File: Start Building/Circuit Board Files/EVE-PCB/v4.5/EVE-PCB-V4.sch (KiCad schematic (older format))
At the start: 37 parts, among them J1 PJ-102AH, J2 2x20 Male Header, J3 1725669, Q1 UA7805CKCT, Q6 DMN10H220L-7, Q7 DMN10H220L-7, U1 PCA9685PW, U2 ADS1115IDGSR, U3 LM324DR

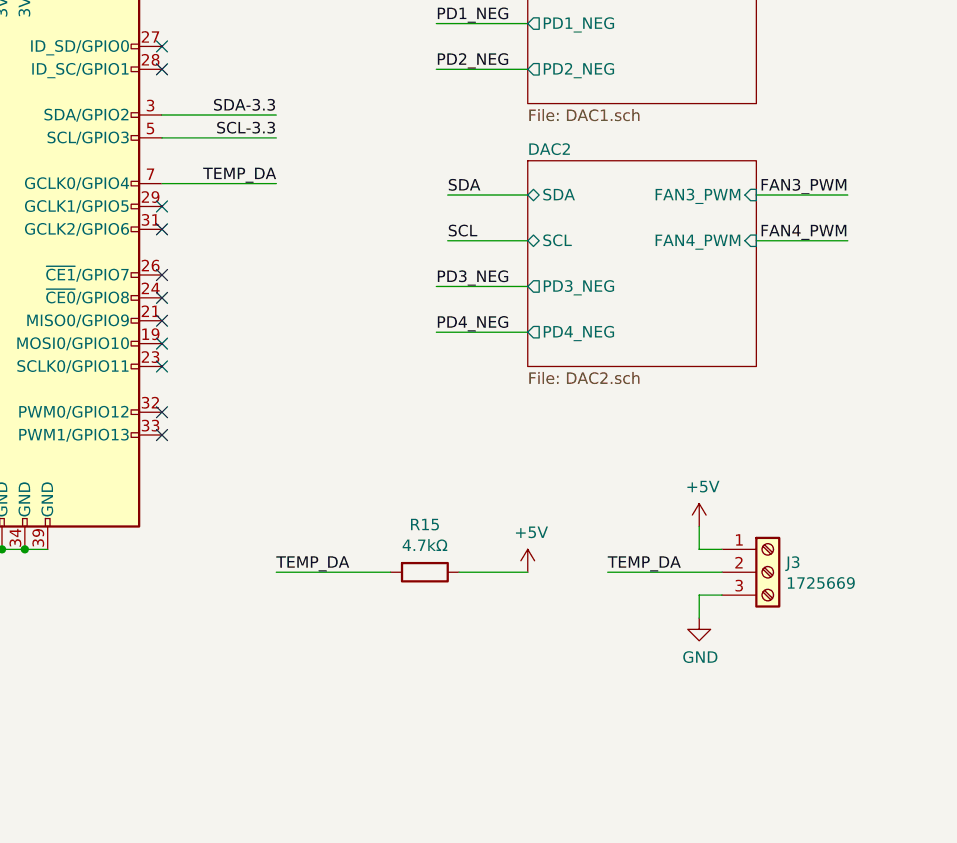
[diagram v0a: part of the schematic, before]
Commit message: PCB v4.5 temp sensor PCB addition
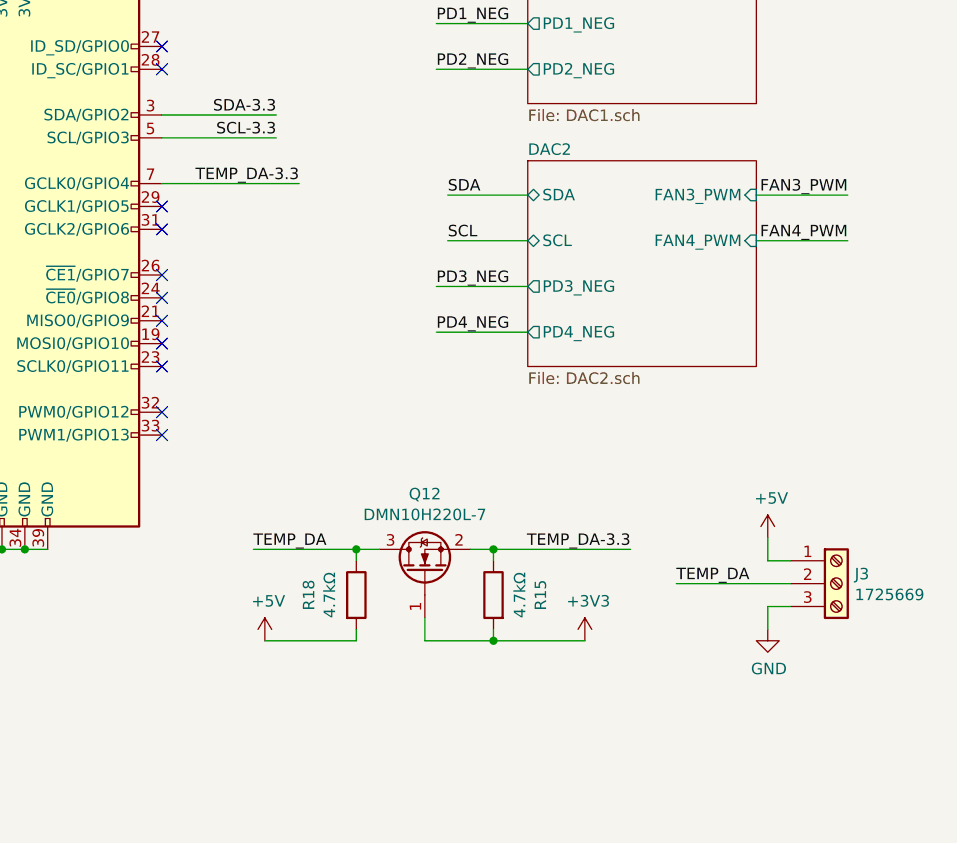
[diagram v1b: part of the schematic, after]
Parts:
- added Q12: DMN10H220L-7, Package_TO_SOT_SMD:SOT-23, symbol Transistor_FET:DMN10H220L
- added R18: 4.7kΩ, Resistor_SMD:R_0402_1005Metric, symbol Device:R
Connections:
- net +3V3: now also R15.2, Q12.1 (G)
- net +5V: now also R18.2; no longer R15.1
- net TEMP_DA: now also Q12.3 (D), R18.1; no longer J2.7 (GCLK0/GPIO4), R15.2
- new net TEMP_DA-3.3: J2.7 (GCLK0/GPIO4), Q12.2 (S), R15.1
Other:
- moved on the sheet: J3, R15
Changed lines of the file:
@@
 L Connector:Screw_Terminal_01x03 J3
 U 1 1 5EC87689
-P 10200 5600
-F 0 "J3" H 10280 5642 50  0000 L CNN
-F 1 "1725669" H 10280 5551 50  0000 L CNN
-F 2 "1725669andothers:1725669" H 10200 5600 50  0001 C CNN
-F 3 "1935174" H 10200 5600 50  0001 C CNN
-	1    10200 5600
+P 10500 5650
+F 0 "J3" H 10580 5692 50  0000 L CNN
+F 1 "1725669" H 10580 5601 50  0000 L CNN
+F 2 "1725669andothers:1725669" H 10500 5650 50  0001 C CNN
+F 3 "1935174" H 10500 5650 50  0001 C CNN
+	1    10500 5650
 	1    0    0    -1
 $EndComp
@@
 L EVE-PCB-V4-rescue:+5V-power-EVE-PCB-rescue #PWR07
 U 1 1 5ECA1474
-P 9900 5400
-F 0 "#PWR07" H 9900 5250 50  0001 C CNN
-F 1 "+5V" H 9915 5573 50  0000 C CNN
-F 2 "" H 9900 5400 50  0001 C CNN
-F 3 "" H 9900 5400 50  0001 C CNN
-	1    9900 5400
+P 10200 5450
+F 0 "#PWR07" H 10200 5300 50  0001 C CNN
+F 1 "+5V" H 10215 5623 50  0000 C CNN
+F 2 "" H 10200 5450 50  0001 C CNN
+F 3 "" H 10200 5450 50  0001 C CNN
+	1    10200 5450
 	1    0    0    -1
 $EndComp
-Text Label 8050 3900 2    50   ~ 0
+Text Label 8150 3900 2    50   ~ 0
+TEMP_DA-3.3
+Text Label 9800 5650 0    50   ~ 0
 TEMP_DA
 Wire Wire Line
-	8050 3900 7550 3900
-Text Label 9500 5600 0    50   ~ 0
-TEMP_DA
+	10300 5650 9800 5650
 Wire Wire Line
-	10000 5600 9500 5600
+	10200 5450 10200 5550
 Wire Wire Line
-	9900 5400 9900 5500
-Wire Wire Line
-	9900 5500 10000 5500
+	10200 5550 10300 5550
 $Comp
 L EVE-PCB-V4-rescue:GND-power-EVE-PCB-rescue #PWR08
 U 1 1 5ED40817
-P 9900 5800
-F 0 "#PWR08" H 9900 5550 50  0001 C CNN
-F 1 "GND" H 9905 5627 50  0000 C CNN
-F 2 "" H 9900 5800 50  0001 C CNN
-F 3 "" H 9900 5800 50  0001 C CNN
-	1    9900 5800
+P 10200 5850
+F 0 "#PWR08" H 10200 5600 50  0001 C CNN
+F 1 "GND" H 10205 5677 50  0000 C CNN
+F 2 "" H 10200 5850 50  0001 C CNN
+F 3 "" H 10200 5850 50  0001 C CNN
+	1    10200 5850
 	1    0    0    -1
 $EndComp
 Wire Wire Line
-	9900 5800 9900 5700
+	10200 5850 10200 5750
 Wire Wire Line
-	9900 5700 10000 5700
-Text Label 8050 5600 0    50   ~ 0
-TEMP_DA
-Wire Wire Line
-	8550 5600 8050 5600
+	10200 5750 10300 5750
 $Comp
 L Device:R R15
 U 1 1 5ED69B49
-P 8700 5600
-F 0 "R15" V 8493 5600 50  0000 C CNN
-F 1 "4.7kΩ" V 8584 5600 50  0000 C CNN
-F 2 "Resistor_SMD:R_0402_1005Metric" V 8630 5600 50  0001 C CNN
-F 3 "0402WGF4701TCE" H 8700 5600 50  0001 C CNN
-F 4 "C25900" V 8700 5600 50  0001 C CNN "LCSC"
-F 5 "0402" H 8700 5600 50  0001 C CNN "Package"
-F 6 "Low" V 8700 5600 50  0001 C CNN "Power"
-	1    8700 5600
-	0    1    1    0
+P 9000 5700
+F 0 "R15" V 8793 5700 50  0000 C CNN
+F 1 "4.7kΩ" V 8884 5700 50  0000 C CNN
+F 2 "Resistor_SMD:R_0402_1005Metric" V 8930 5700 50  0001 C CNN
+F 3 "0402WGF4701TCE" H 9000 5700 50  0001 C CNN
+F 4 "C25900" V 9000 5700 50  0001 C CNN "LCSC"
+F 5 "0402" H 9000 5700 50  0001 C CNN "Package"
+F 6 "Low" V 9000 5700 50  0001 C CNN "Power"
+	1    9000 5700
+	-1   0    0    -1
 $EndComp
+Wire Wire Line
+	8900 5500 9000 5500
 $Comp
-L EVE-PCB-V4-rescue:+5V-power-EVE-PCB-rescue #PWR03
-U 1 1 5ED75219
-P 9150 5600
-F 0 "#PWR03" H 9150 5450 50  0001 C CNN
-F 1 "+5V" H 9165 5773 50  0000 C CNN
-F 2 "" H 9150 5600 50  0001 C CNN
-F 3 "" H 9150 5600 50  0001 C CNN
-	1    9150 5600
+L EVE-PCB-V4-rescue:+3V3-power-EVE-PCB-rescue #PWR016
+U 1 1 5EDD4AD6
+P 9400 5900
+F 0 "#PWR016" H 9400 5750 50  0001 C CNN
+F 1 "+3V3" H 9415 6073 50  0000 C CNN
+F 2 "" H 9400 5900 50  0001 C CNN
+F 3 "" H 9400 5900 50  0001 C CNN
+	1    9400 5900
 	1    0    0    -1
 $EndComp
 Wire Wire Line
-	8850 5600 9150 5600
+	9000 5550 9000 5500
+Wire Wire Line
+	9000 5850 9000 5900
+Connection ~ 9000 5900
+$Comp
+L EVE-PCB-V4-rescue:+5V-power-EVE-PCB-rescue #PWR03
+U 1 1 5EDD4AE0
+P 8000 5900
+F 0 "#PWR03" H 8000 5750 50  0001 C CNN
+F 1 "+5V" H 8015 6073 50  0000 C CNN
+F 2 "" H 8000 5900 50  0001 C CNN
+F 3 "" H 8000 5900 50  0001 C CNN
+	1    8000 5900
+	1    0    0    -1
+$EndComp
+Wire Wire Line
+	8400 5900 8400 5850
+Wire Wire Line
+	8400 5550 8400 5500
+Connection ~ 8400 5500
+Wire Wire Line
+	8400 5500 8500 5500
+Wire Wire Line
+	8000 5900 8400 5900
+Wire Wire Line
+	9000 5900 9400 5900
+Connection ~ 9000 5500
+$Comp
+L Transistor_FET:DMN10H220L Q12
+U 1 1 5EDD4B03
+P 8700 5600
+F 0 "Q12" V 9042 5600 50  0000 C CNN
+F 1 "DMN10H220L-7" V 8951 5600 50  0000 C CNN
+F 2 "Package_TO_SOT_SMD:SOT-23" H 8900 5525 50  0001 L CIN
+F 3 "DMN10H220L-7" H 8700 5600 50  0001 L CNN
+F 4 "C102615" H 8700 5600 50  0001 C CNN "LCSC"
+F 5 "SOT-23-3" H 8700 5600 50  0001 C CNN "Package"
+	1    8700 5600
+	0    -1   -1   0
+$EndComp
+Wire Wire Line
+	8700 5800 8700 5900
+Wire Wire Line
+	8700 5900 9000 5900
+$Comp
+L Device:R R18
+U 1 1 5EE07A53
+P 8400 5700
+F 0 "R18" V 8193 5700 50  0000 C CNN
+F 1 "4.7kΩ" V 8284 5700 50  0000 C CNN
+F 2 "Resistor_SMD:R_0402_1005Metric" V 8330 5700 50  0001 C CNN
+F 3 "0402WGF4701TCE" H 8400 5700 50  0001 C CNN
+F 4 "C25900" V 8400 5700 50  0001 C CNN "LCSC"
+F 5 "0402" H 8400 5700 50  0001 C CNN "Package"
+F 6 "Low" V 8400 5700 50  0001 C CNN "Power"
+	1    8400 5700
+	1    0    0    -1
+$EndComp
+Text Label 7950 5500 0    50   ~ 0
+TEMP_DA
+Wire Wire Line
+	7950 5500 8400 5500
+Text Label 9600 5500 2    50   ~ 0
+TEMP_DA-3.3
+Wire Wire Line
+	9000 5500 9600 5500
+Wire Wire Line
+	7550 3900 8150 3900
 $EndSCHEMATC

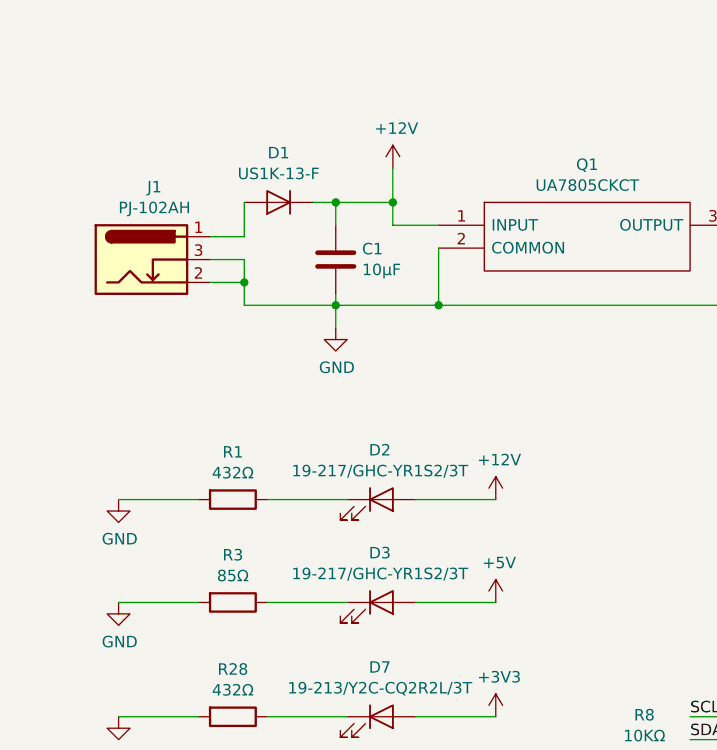
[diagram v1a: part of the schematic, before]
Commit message: Updates to v4.5 and include support for ADS1115
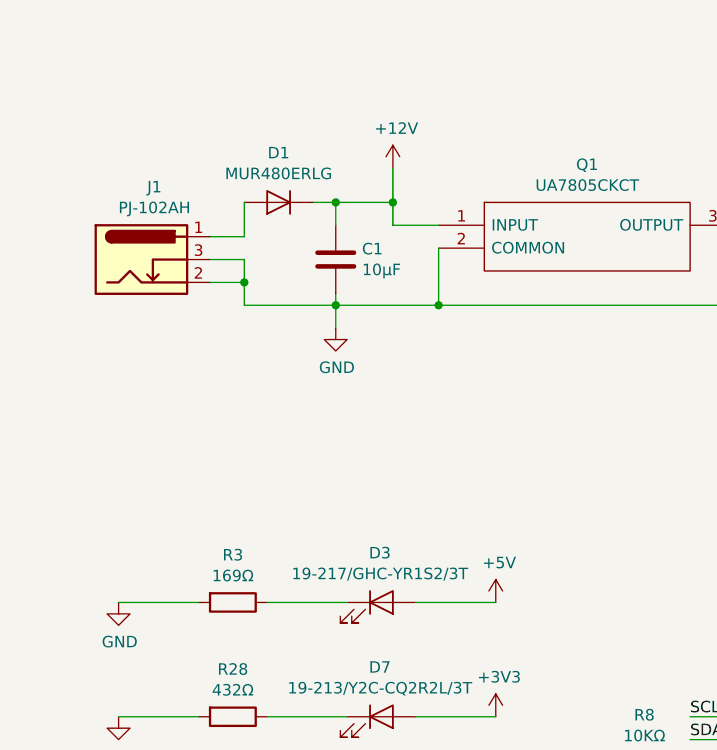
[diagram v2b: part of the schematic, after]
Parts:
- removed D2: 19-217/GHC-YR1S2/3T, LED_SMD:LED_0603_1608Metric, symbol Device:LED
- removed R1: 432Ω, Resistor_SMD:R_1206_3216Metric, symbol Device:R
- C6: footprint Capacitor_SMD:C_0402_1005Metric -> Capacitor_SMD:C_0603_1608Metric; LCSC C29266 -> C5673; Package 0402 -> 0603
- D1: value US1K-13-F -> MUR480ERLG; footprint Diode_SMD:D_SMA -> Diode_THT:D_DO-201AE_P3.81mm_Vertical_AnodeUp; LCSC C110532 -> (none)
- R3: value 85Ω -> 169Ω; LCSC C17843 -> C17489; Power 0.034 -> 0.017
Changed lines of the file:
@@
 	2350 3450 2550 3450
-$Comp
-L EVE-PCB-V4-rescue:+12V-power-EVE-PCB-rescue #PWR?
-U 1 1 5EBD3BD1
-P 2800 4650
-AR Path="/5CA7DFAE/5EBD3BD1" Ref="#PWR?"  Part="1"
-AR Path="/5EBD3BD1" Ref="#PWR06"  Part="1"
-F 0 "#PWR06" H 2800 4500 50  0001 C CNN
-F 1 "+12V" H 2815 4823 50  0000 C CNN
-F 2 "" H 2800 4650 50  0001 C CNN
-F 3 "" H 2800 4650 50  0001 C CNN
-	1    2800 4650
-	1    0    0    -1
-$EndComp
-$Comp
-L EVE-PCB-V4-rescue:GND-power-EVE-PCB-rescue #PWR01
-U 1 1 5EC07E2B
-P 1150 4650
-F 0 "#PWR01" H 1150 4400 50  0001 C CNN
-F 1 "GND" H 1155 4477 50  0000 C CNN
-F 2 "" H 1150 4650 50  0001 C CNN
-F 3 "" H 1150 4650 50  0001 C CNN
-	1    1150 4650
-	1    0    0    -1
-$EndComp
-Wire Wire Line
-	1150 4650 1500 4650
-Wire Wire Line
-	2450 4650 2800 4650
-Wire Wire Line
-	1800 4650 2150 4650
 $Comp
 L EVE-PCB-V4-rescue:GND-power-EVE-PCB-rescue #PWR010
@@
 P 1650 5100
 F 0 "R3" V 1443 5100 50  0000 C CNN
-F 1 "85Ω" V 1534 5100 50  0000 C CNN
+F 1 "169Ω" V 1534 5100 50  0000 C CNN
 F 2 "Resistor_SMD:R_0805_2012Metric" V 1580 5100 50  0001 C CNN
-F 3 "0805W8F845JT5E" H 1650 5100 50  0001 C CNN
-F 4 "C17843" V 1650 5100 50  0001 C CNN "LCSC"
+F 3 "0805W8F1690T5E" H 1650 5100 50  0001 C CNN
+F 4 "C17489" V 1650 5100 50  0001 C CNN "LCSC"
 F 5 "0805" H 1650 5100 50  0001 C CNN "Package"
-F 6 "0.034" V 1650 5100 50  0001 C CNN "Power"
+F 6 "0.017" V 1650 5100 50  0001 C CNN "Power"
 	1    1650 5100
-	0    1    1    0
-$EndComp
-$Comp
-L Device:LED D2
-U 1 1 5EB9661E
-P 2300 4650
-F 0 "D2" H 2293 4866 50  0000 C CNN
-F 1 "19-217/GHC-YR1S2/3T" H 2293 4775 50  0000 C CNN
-F 2 "LED_SMD:LED_0603_1608Metric" H 2300 4650 50  0001 C CNN
-F 3 "19-217/GHC-YR1S2/3T (Green)" H 2300 4650 50  0001 C CNN
-F 4 "C72043" H 2300 4650 50  0001 C CNN "LCSC"
-F 5 "LED_0603" H 2300 4650 50  0001 C CNN "Package"
-	1    2300 4650
-	1    0    0    -1
-$EndComp
-$Comp
-L Device:R R1
-U 1 1 5EBF7816
-P 1650 4650
-F 0 "R1" V 1443 4650 50  0000 C CNN
-F 1 "432Ω" V 1534 4650 50  0000 C CNN
-F 2 "Resistor_SMD:R_1206_3216Metric" V 1580 4650 50  0001 C CNN
-F 3 "1206W4F4320T5E" H 1650 4650 50  0001 C CNN
-F 4 "C247258" V 1650 4650 50  0001 C CNN "LCSC"
-F 5 "1206" H 1650 4650 50  0001 C CNN "Package"
-F 6 "0.174" V 1650 4650 50  0001 C CNN "Power"
-	1    1650 4650
 	0    1    1    0
 $EndComp
@@
 P 1850 3350
 F 0 "D1" H 1850 3134 50  0000 C CNN
-F 1 "US1K-13-F" H 1850 3225 50  0000 C CNN
-F 2 "Diode_SMD:D_SMA" H 1850 3350 50  0001 C CNN
-F 3 "US1K-13-F" H 1850 3350 50  0001 C CNN
-F 4 "C110532" H 1850 3350 50  0001 C CNN "LCSC"
+F 1 "MUR480ERLG" H 1850 3225 50  0000 C CNN
+F 2 "Diode_THT:D_DO-201AE_P3.81mm_Vertical_AnodeUp" H 1850 3350 50  0001 C CNN
+F 3 "MUR480ERLG" H 1850 3350 50  0001 C CNN
+F 4 "" H 1850 3350 50  0001 C CNN "LCSC"
 F 5 "SMA,DO-214AC" H 1850 3350 50  0001 C CNN "Package"
 	1    1850 3350
@@
 F 0 "C6" H 4615 3646 50  0000 L CNN
 F 1 "1μF" H 4615 3555 50  0000 L CNN
-F 2 "Capacitor_SMD:C_0402_1005Metric" H 4538 3450 50  0001 C CNN
-F 3 "CL05A105KO5NNNC" H 4500 3600 50  0001 C CNN
-F 4 "C29266" H 4500 3600 50  0001 C CNN "LCSC"
-F 5 "0402" H 4500 3600 50  0001 C CNN "Package"
+F 2 "Capacitor_SMD:C_0603_1608Metric" H 4538 3450 50  0001 C CNN
+F 3 "CL10A105KA8NNNC" H 4500 3600 50  0001 C CNN
+F 4 "C5673" H 4500 3600 50  0001 C CNN "LCSC"
+F 5 "0603" H 4500 3600 50  0001 C CNN "Package"
 	1    4500 3600
 	1    0    0    -1
